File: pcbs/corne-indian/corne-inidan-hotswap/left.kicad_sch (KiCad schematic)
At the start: 51 parts, among them SW1 SW_Push, SW10 SW_Push, SW11 SW_Push, SW12 SW_Push, SW13 SW_Push, SW14 SW_Push, SW15 SW_Push, SW16 SW_Push, SW17 SW_Push, SW18 SW_Push, SW19 SW_Push, SW2 SW_Push, SW20 SW_Push, SW21 SW_Push, SW3 SW_Push, SW4 SW_Push, SW5 SW_Push, SW6 SW_Push, SW7 SW_Push, SW8 SW_Push, SW9 SW_Push

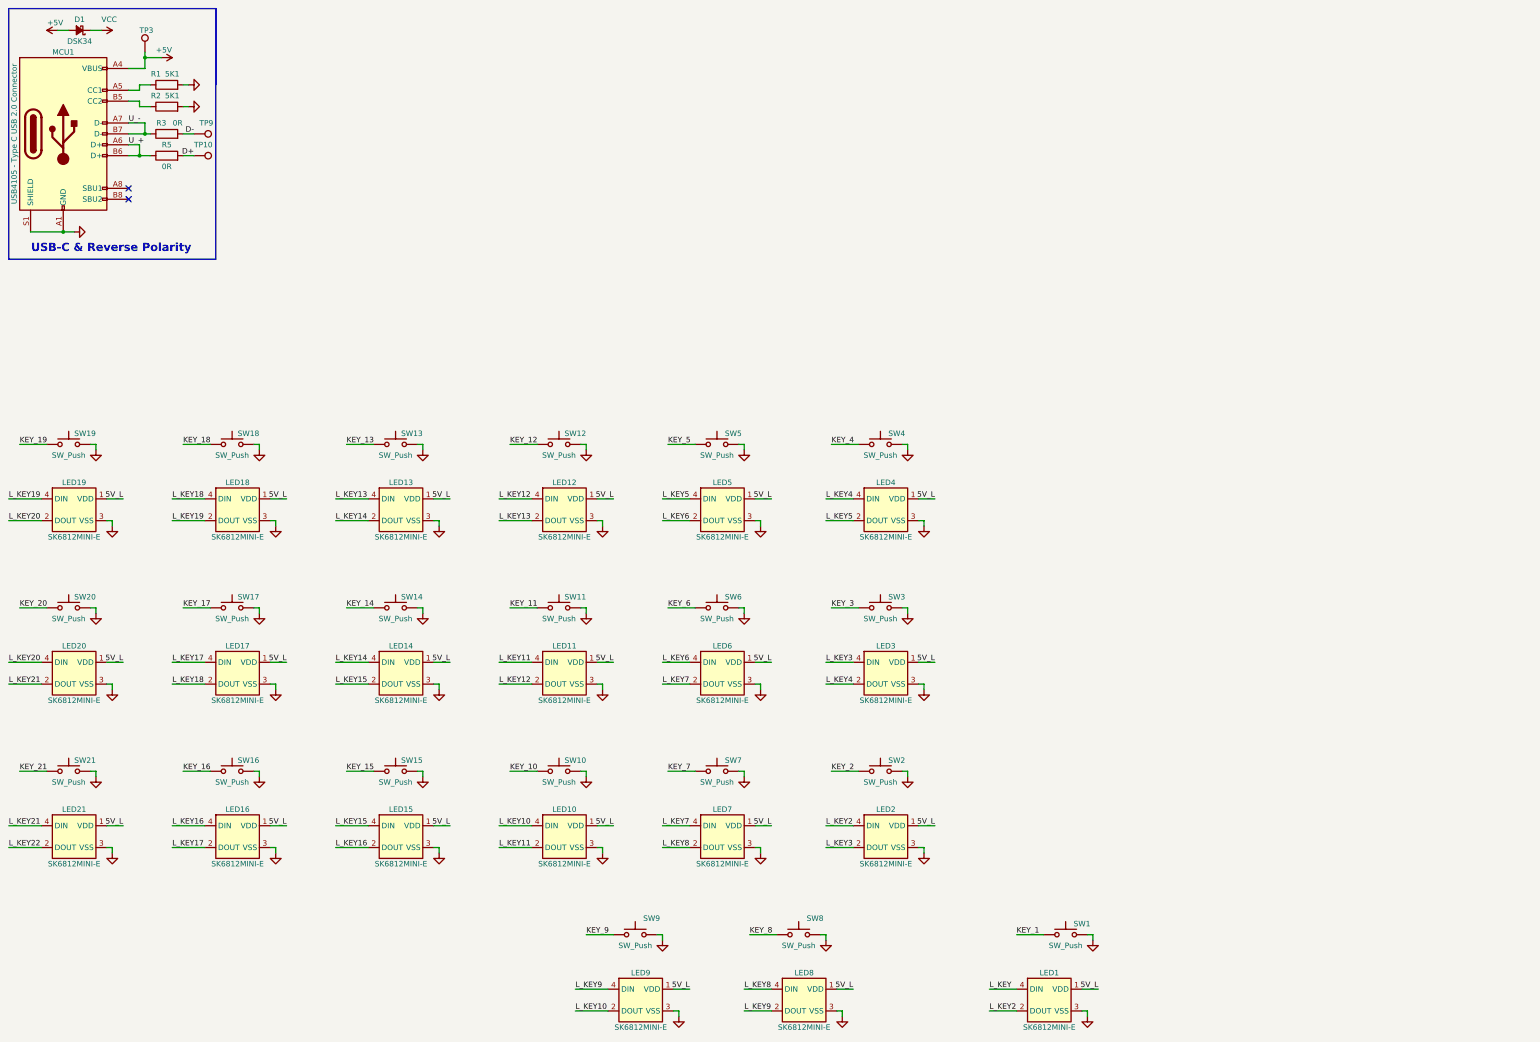
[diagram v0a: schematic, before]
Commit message: Rp2040 added to the shematic need to map to all Key Switch pins
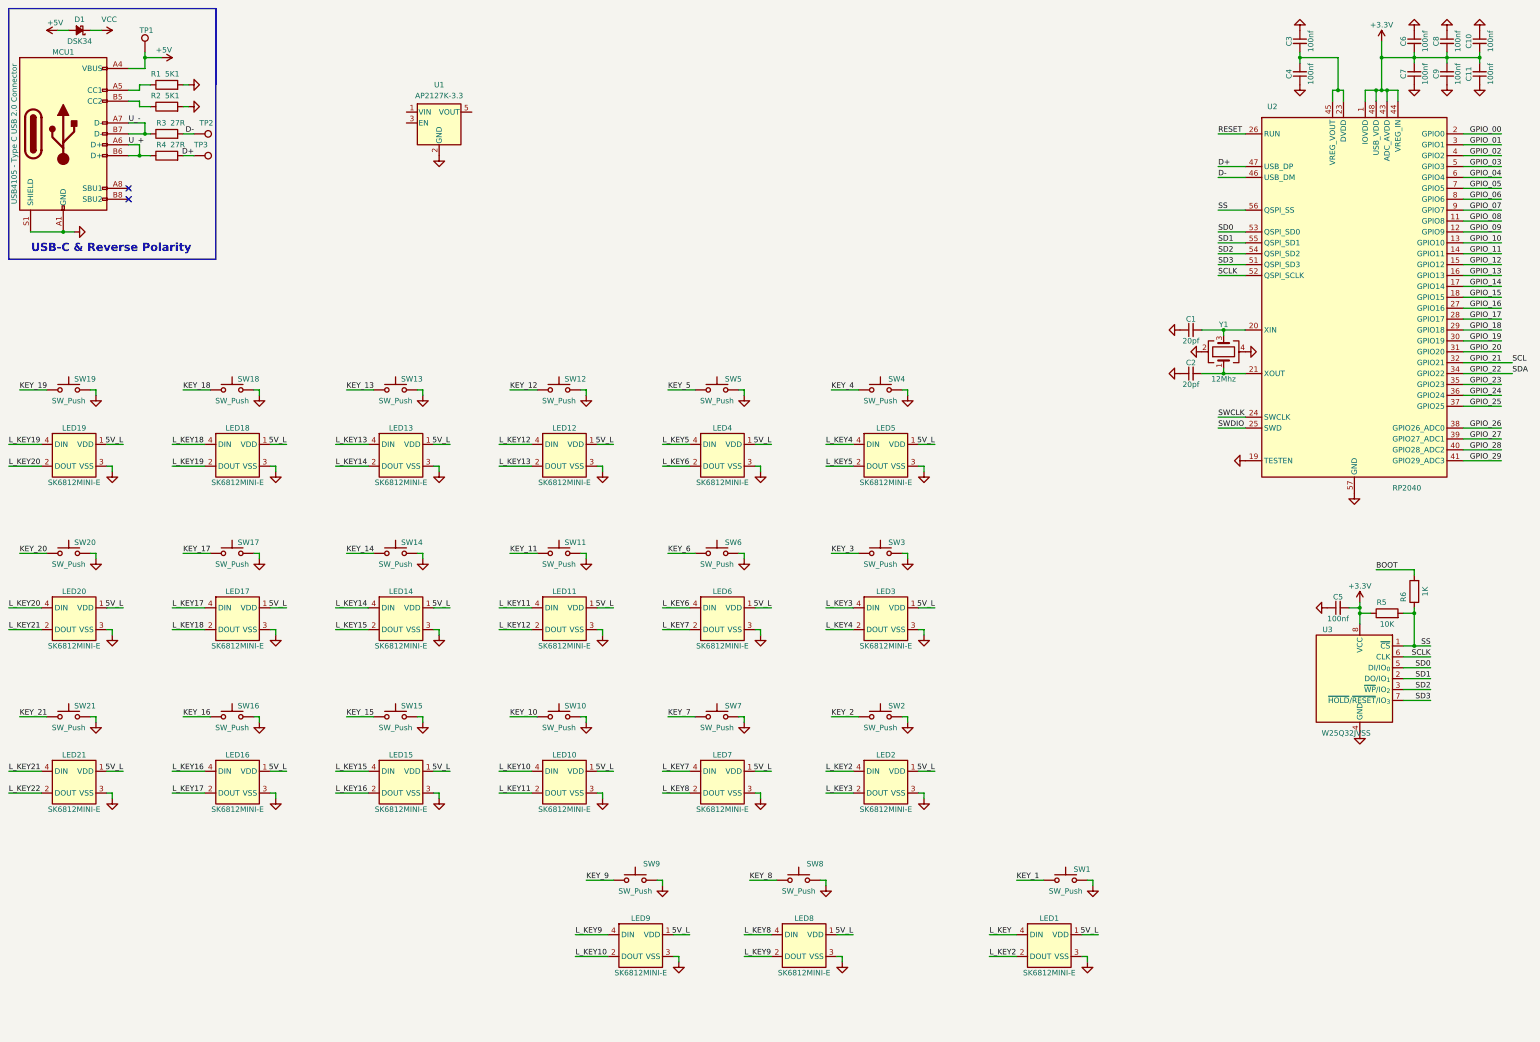
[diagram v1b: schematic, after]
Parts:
- added C1, C2: 20pf, Capacitor_SMD:C_0603_1608Metric, symbol Device:C_Small
- added C10, C11, C3, C4, C5, C6, C7, C8, C9: 100nf, Capacitor_SMD:C_0603_1608Metric, symbol Device:C_Small
- added R4: 27R, Resistor_SMD:R_0603_1608Metric, symbol Device:R
- added R6: 1K, Resistor_SMD:R_0603_1608Metric, symbol Device:R
- added U1: AP2127K-3.3, Package_TO_SOT_SMD:SOT-23-5, symbol Regulator_Linear:AP2127K-3.3
- added U2: RP2040, Package_DFN_QFN:QFN-56-1EP_7x7mm_P0.4mm_EP3.2x3.2mm, symbol MCU_RaspberryPi:RP2040
- added U3: W25Q32JVSS, Package_SO:SOIC-8_5.3x5.3mm_P1.27mm, symbol Memory_Flash:W25Q32JVSS
- added Y1: 12Mhz, Crystal:Crystal_SMD_Abracon_ABM8AIG-4Pin_3.2x2.5mm, symbol Device:Crystal_GND24
- R3: value 0R -> 27R; LCSC_Part C21189 -> (none); Manufacturer_Part_Number MCWR06X000 PTL -> (none); Manufacturer_Part_Number_2 0603WAF0000T5E -> (none)
- R5: value 0R -> 10K; LCSC_Part C21189 -> C25804; Manufacturer_Part_Number MCWR06X000 PTL -> MCWR06X1002FTL; Manufacturer_Part_Number_2 0603WAF0000T5E -> 0603WAF1002T5E
- renumbered LED5 to LED4, LED4 to LED5, TP3 to TP1, TP9 to TP2, TP10 to TP3
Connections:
- net D+: now also R4.2, U2.47 (USB_DP); no longer R5.2
- net D-: now also U2.46 (USB_DM)
- net GND: now also C1.1, C10.1, C11.1, C2.1, C3.1, C4.1, C5.1, C6.1, C7.1, C8.1, C9.1, U1.2 (GND), U2.19 (TESTEN), U2.57 (GND), U3.4 (GND), Y1.2, Y1.4
- net U_+: now also R4.1; no longer R5.1
- new net: C3.2, C4.2, U2.23 (DVDD), U2.45 (VREG_VOUT), U2.50 (DVDD)
- new net: C1.2, U2.20 (XIN), Y1.3
- new net: C2.2, U2.21 (XOUT), Y1.1
- new net +3.3V: C10.2, C11.2, C5.2, C6.2, C7.2, C8.2, C9.2, R5.1, U2.1 (IOVDD), U2.10 (IOVDD), U2.22 (IOVDD), U2.33 (IOVDD), U2.42 (IOVDD), U2.43 (ADC_AVDD), U2.44 (VREG_IN), U2.48 (USB_VDD), U2.49 (IOVDD), U3.8 (VCC)
- new net BOOT: R6.2
- new net GPIO_00: U2.2 (GPIO0)
- new net GPIO_01: U2.3 (GPIO1)
- new net GPIO_02: U2.4 (GPIO2)
- new net GPIO_03: U2.5 (GPIO3)
- new net GPIO_04: U2.6 (GPIO4)
- new net GPIO_05: U2.7 (GPIO5)
- new net GPIO_06: U2.8 (GPIO6)
- new net GPIO_07: U2.9 (GPIO7)
- new net GPIO_08: U2.11 (GPIO8)
- new net GPIO_09: U2.12 (GPIO9)
- new net GPIO_10: U2.13 (GPIO10)
- new net GPIO_11: U2.14 (GPIO11)
- new net GPIO_12: U2.15 (GPIO12)
- new net GPIO_13: U2.16 (GPIO13)
- new net GPIO_14: U2.17 (GPIO14)
- new net GPIO_15: U2.18 (GPIO15)
- new net GPIO_16: U2.27 (GPIO16)
- new net GPIO_17: U2.28 (GPIO17)
- new net GPIO_18: U2.29 (GPIO18)
- new net GPIO_19: U2.30 (GPIO19)
- new net GPIO_20: U2.31 (GPIO20)
- new net GPIO_21: U2.32 (GPIO21)
- new net GPIO_22: U2.34 (GPIO22)
- new net GPIO_23: U2.35 (GPIO23)
- new net GPIO_24: U2.36 (GPIO24)
- new net GPIO_25: U2.37 (GPIO25)
- new net GPIO_26: U2.38 (GPIO26_ADC0)
- new net GPIO_27: U2.39 (GPIO27_ADC1)
- new net GPIO_28: U2.40 (GPIO28_ADC2)
- new net GPIO_29: U2.41 (GPIO29_ADC3)
- new net RESET: U2.26 (RUN)
- new net SCLK: U2.52 (QSPI_SCLK), U3.6 (CLK)
- new net SD0: U2.53 (QSPI_SD0), U3.5 (DI/IO_{0})
- new net SD1: U2.55 (QSPI_SD1), U3.2 (DO/IO_{1})
- new net SD2: U2.54 (QSPI_SD2), U3.3 (~{WP}/IO_{2})
- new net SD3: U2.51 (QSPI_SD3), U3.7 (~{HOLD}/~{RESET}/IO_{3})
- new net SS: R5.2, R6.1, U2.56 (QSPI_SS), U3.1 (~{CS})
- new net SWCLK: U2.24 (SWCLK)
- new net SWDIO: U2.25 (SWD)
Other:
- moved on the sheet: LED10, LED11, LED12, LED13, LED14, LED15, LED16, LED17, LED18, LED19, LED2, LED20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

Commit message: Mid of the renumbering & renaming
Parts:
- added J1: Conn_01x03_Pin, Connector_PinHeader_2.54mm:PinHeader_1x03_P2.54mm_Vertical, symbol Connector:Conn_01x03_Pin
- added J2: Conn_01x04_Pin, Connector_PinHeader_2.54mm:PinHeader_1x04_P2.54mm_Vertical, symbol Connector:Conn_01x04_Pin
- added R7: 10K, Resistor_SMD:R_0603_1608Metric, symbol Device:R
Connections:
- net GPIO_00 is gone; now on net KEY_4: U2.2 (GPIO0)
- net GPIO_01 is gone; now on net KEY_6: U2.3 (GPIO1)
- net GPIO_02 is gone; now on net KEY_3: U2.4 (GPIO2)
- net GPIO_03 is gone; now on net KEY_7: U2.5 (GPIO3)
- net GPIO_09 is gone; now on net KEY_2: U2.12 (GPIO9)
- net GPIO_11 is gone; now on net KEY_1: U2.14 (GPIO11)
- net GPIO_14 is gone; now on net KEY_9: U2.17 (GPIO14)
- net GPIO_15 is gone; now on net KEY_8: U2.18 (GPIO15)
- net GPIO_16 is gone; now on net KEY_16: U2.27 (GPIO16)
- net GPIO_17 is gone; now on net KEY_21: U2.28 (GPIO17)
- net GPIO_18 is gone; now on net KEY_17: U2.29 (GPIO18)
- net GPIO_19 is gone; now on net KEY_20: U2.30 (GPIO19)
- net GPIO_20 is gone; now on net KEY_18: U2.31 (GPIO20)
- net GPIO_22 is gone; now on net KEY_19: U2.34 (GPIO22)
- net GPIO_23 is gone; now on net KEY_13: U2.35 (GPIO23)
- net GPIO_24 is gone; now on net KEY_14: U2.36 (GPIO24)
- net GPIO_25 is gone; now on net KEY_15: U2.37 (GPIO25)
- net GPIO_26 is gone; now on net KEY_12: U2.38 (GPIO26_ADC0)
- net GPIO_27 is gone; now on net KEY_11: U2.39 (GPIO27_ADC1)
- net GPIO_28 is gone; now on net KEY_10: U2.40 (GPIO28_ADC2)
- net GPIO_29 is gone; now on net KEY_5: U2.41 (GPIO29_ADC3)
- net +3.3V: now also R7.2
- net D+: now also R3.2; no longer R4.2, TP3.1
- net D-: now also R4.2; no longer R3.2, TP2.1
- net U_+: now also R3.1, TP3.1; no longer R4.1
- net U_-: now also R4.1, TP2.1; no longer R3.1
- net GPIO_04: no longer names the net of U2.6 (GPIO4)
- net GPIO_05: no longer names the net of U2.7 (GPIO5)
- net GPIO_06: no longer names the net of U2.8 (GPIO6)
- net GPIO_07: no longer names the net of U2.9 (GPIO7)
- net GPIO_08: no longer names the net of U2.11 (GPIO8)
- net GPIO_10: no longer names the net of U2.13 (GPIO10)
- net GPIO_12: no longer names the net of U2.15 (GPIO12)
- net GPIO_13: no longer names the net of U2.16 (GPIO13)
- net GPIO_21: no longer names the net of U2.32 (GPIO21)
- net GPIO_21: now also R7.1
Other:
- note added: "Flash Memory"
- note added: "MCU RP2040"
- note added: "SPLIT_HAND_PIN"
- moved on the sheet: C1, C10, C11, C2, C3, C4, C5, C6, C7, C8, C9, R3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

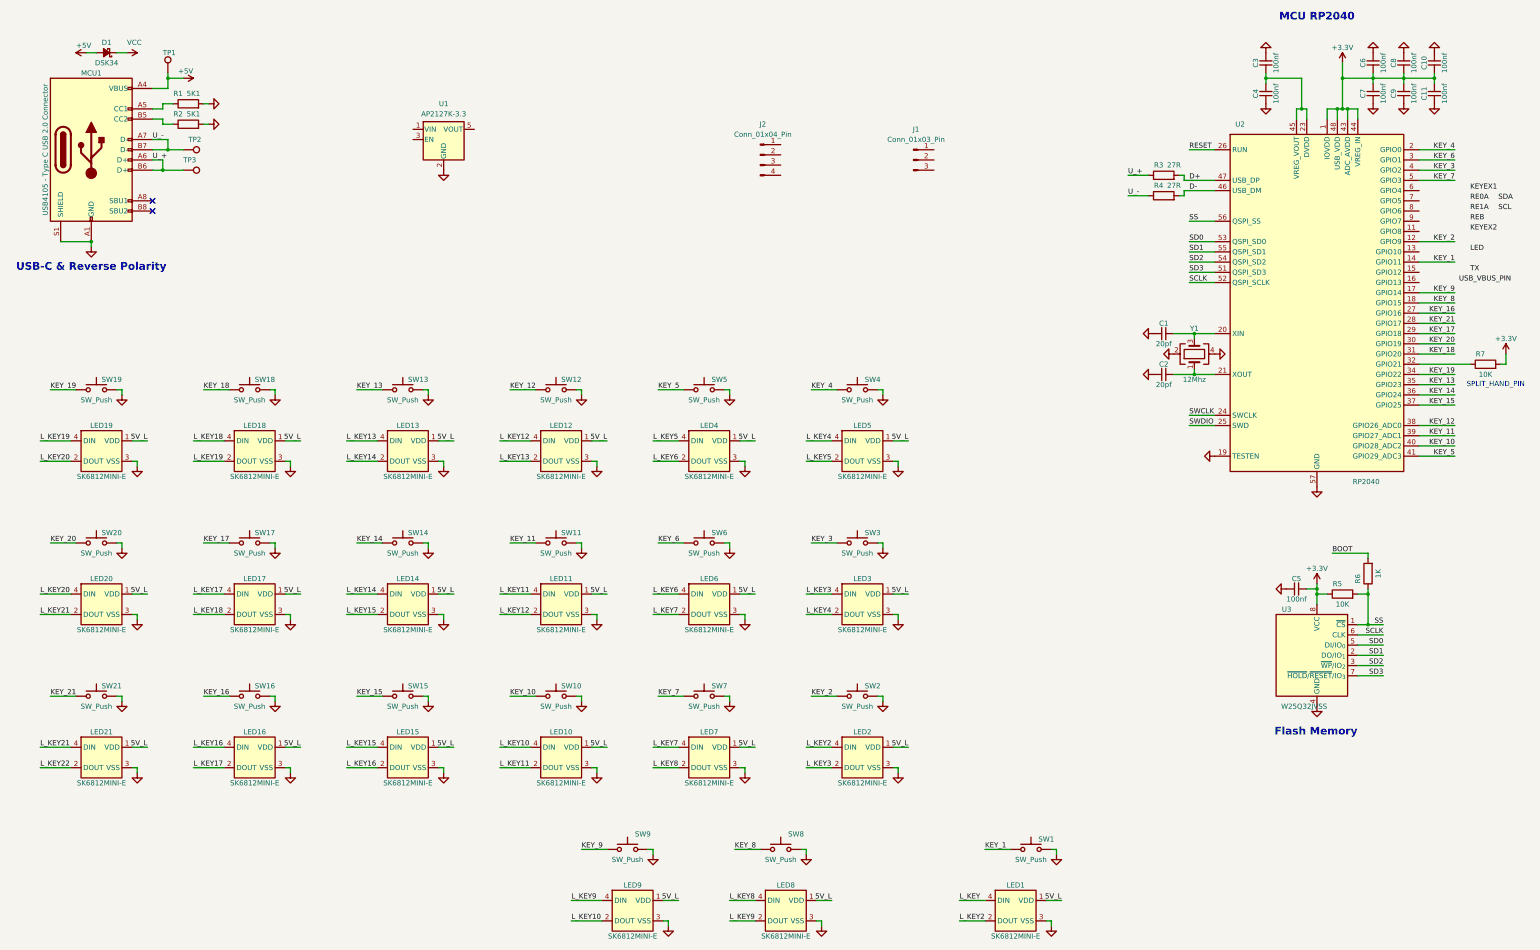
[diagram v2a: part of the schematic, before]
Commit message: Mid of the Placement still Rotary encoder is not done
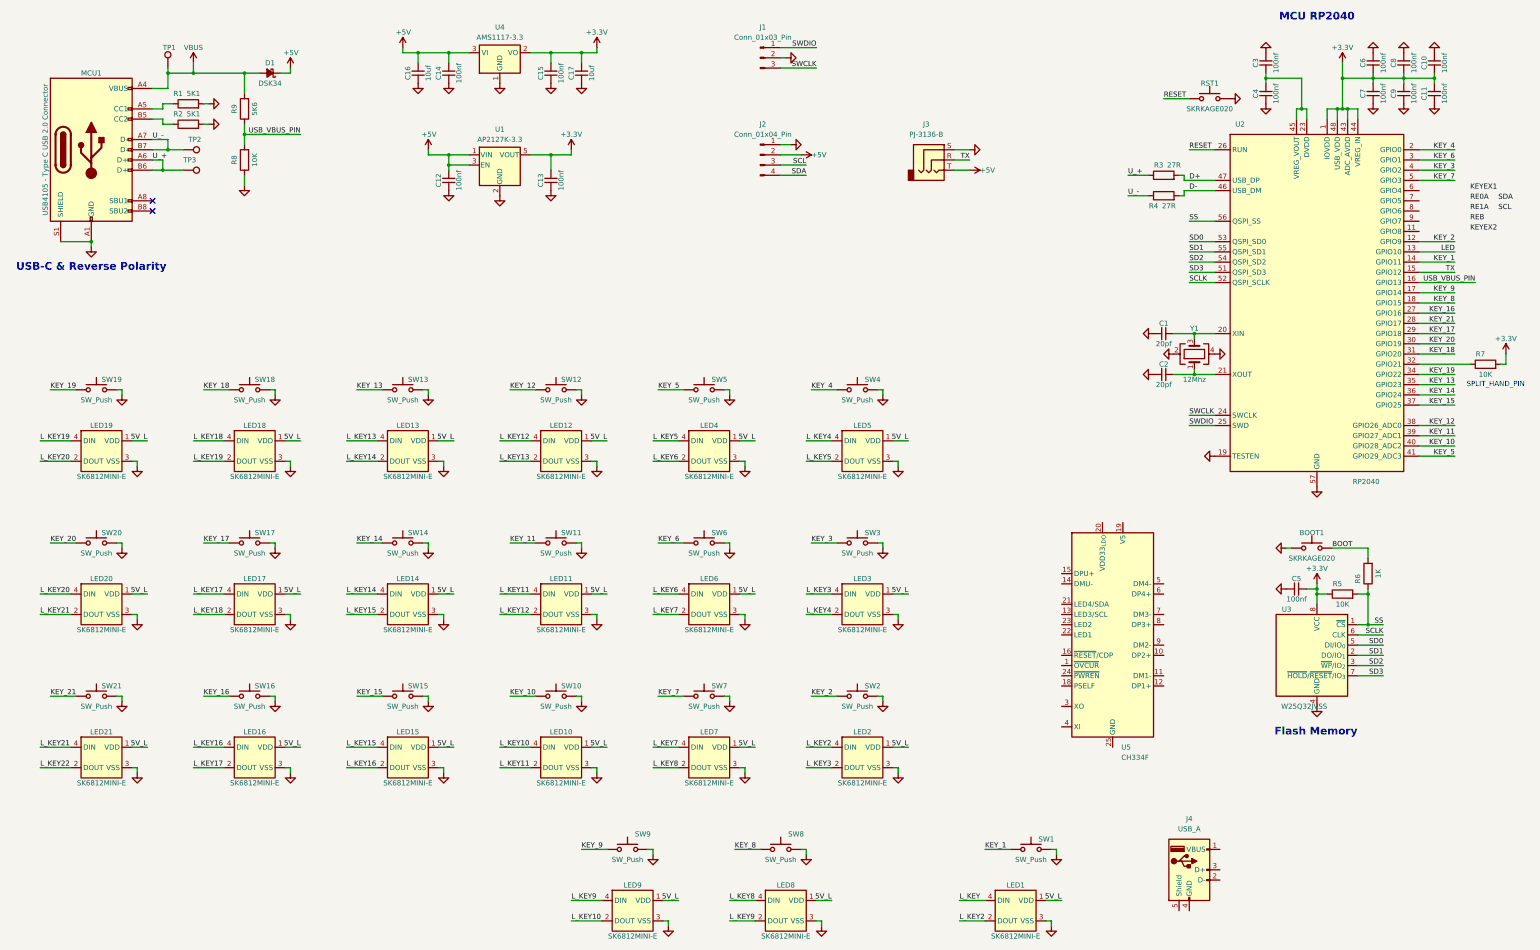
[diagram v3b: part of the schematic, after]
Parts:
- added BOOT1, RST1: SKRKAGE020, Button:SW_Push_SPST_NO_Alps_SKRK, symbol Switch:SW_Push
- added C12, C13, C14, C15: 100nf, Capacitor_SMD:C_0603_1608Metric, symbol Device:C_Small
- added C16, C17: 10uf, Capacitor_SMD:C_0603_1608Metric, symbol Device:C_Small
- added J3: PJ-3136-B, Conn_Audio:PJ-3136-B, symbol Connector_Audio:AudioJack3
- added J4: USB_A, Connector_USB:USB_A_Molex_67643_Horizontal, symbol Connector:USB_A
- added R8: 10K, Resistor_SMD:R_0603_1608Metric, symbol Device:R
- added R9: 5K6, Resistor_SMD:R_0603_1608Metric, symbol Device:R
- added U4: AMS1117-3.3, Package_TO_SOT_SMD:SOT-223-3_TabPin2, symbol Regulator_Linear:AMS1117-3.3
- added U5: CH334F, Package_DFN_QFN:QFN-24-1EP_4x4mm_P0.5mm_EP2.7x2.7mm, symbol Interface_USB:CH334F
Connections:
- net VCC is gone; now on net +5V: D1.1 (K)
- net +3.3V: now also U1.5 (VOUT), C13.2, C15.2, C17.2, U4.2 (VO)
- net +5V: now also J2.2 (Pin_2), U1.1 (VIN), U1.3 (EN), C12.2, C14.2, C16.2, J3.T, U4.3 (VI); no longer D1.2 (A), MCU1.A4 (VBUS), MCU1.A9 (VBUS), MCU1.B4 (VBUS), MCU1.B9 (VBUS), TP1.1
- net BOOT: now also BOOT1.1
- net GND: now also J1.2 (Pin_2), J2.1 (Pin_1), BOOT1.2, C12.1, C13.1, C14.1, C15.1, C16.1, C17.1, J3.S, R8.1, RST1.2, U4.1 (GND)
- net LED: now also U2.13 (GPIO10)
- net RESET: now also RST1.1
- net SCL: now also J2.3 (Pin_3)
- net SDA: now also J2.4 (Pin_4)
- net SWCLK: now also J1.3 (Pin_3)
- net SWDIO: now also J1.1 (Pin_1)
- net TX: now also U2.15 (GPIO12), J3.R
- net USB_VBUS_PIN: now also U2.16 (GPIO13), R8.2, R9.1
- new net VBUS: D1.2 (A), MCU1.A4 (VBUS), MCU1.A9 (VBUS), MCU1.B4 (VBUS), MCU1.B9 (VBUS), R9.2, TP1.1
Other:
- moved on the sheet: D1, J1, TP1, U1
